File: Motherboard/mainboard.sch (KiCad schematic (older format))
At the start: 44 parts, among them IC1 BMX160, J1 Conn_01x01, J2 10118194-0001LF, J28 Conn_01x01, J29 Conn_01x01, J3 Micro_SD_Card, J30 Conn_01x01, J4 xf2m-2415-1a, J5 XF2M-1015-1A, SW1 KMR231NG LFS, U1 RFM95W-915S2, U2 ATSAMD51G_TQFN48, U4 TPS82740BSIPR, U6 MAX708RESA-T, U8 RFM95W-915S2, X1 ANTENNA_U.FL, X2 ANTENNA_U.FL

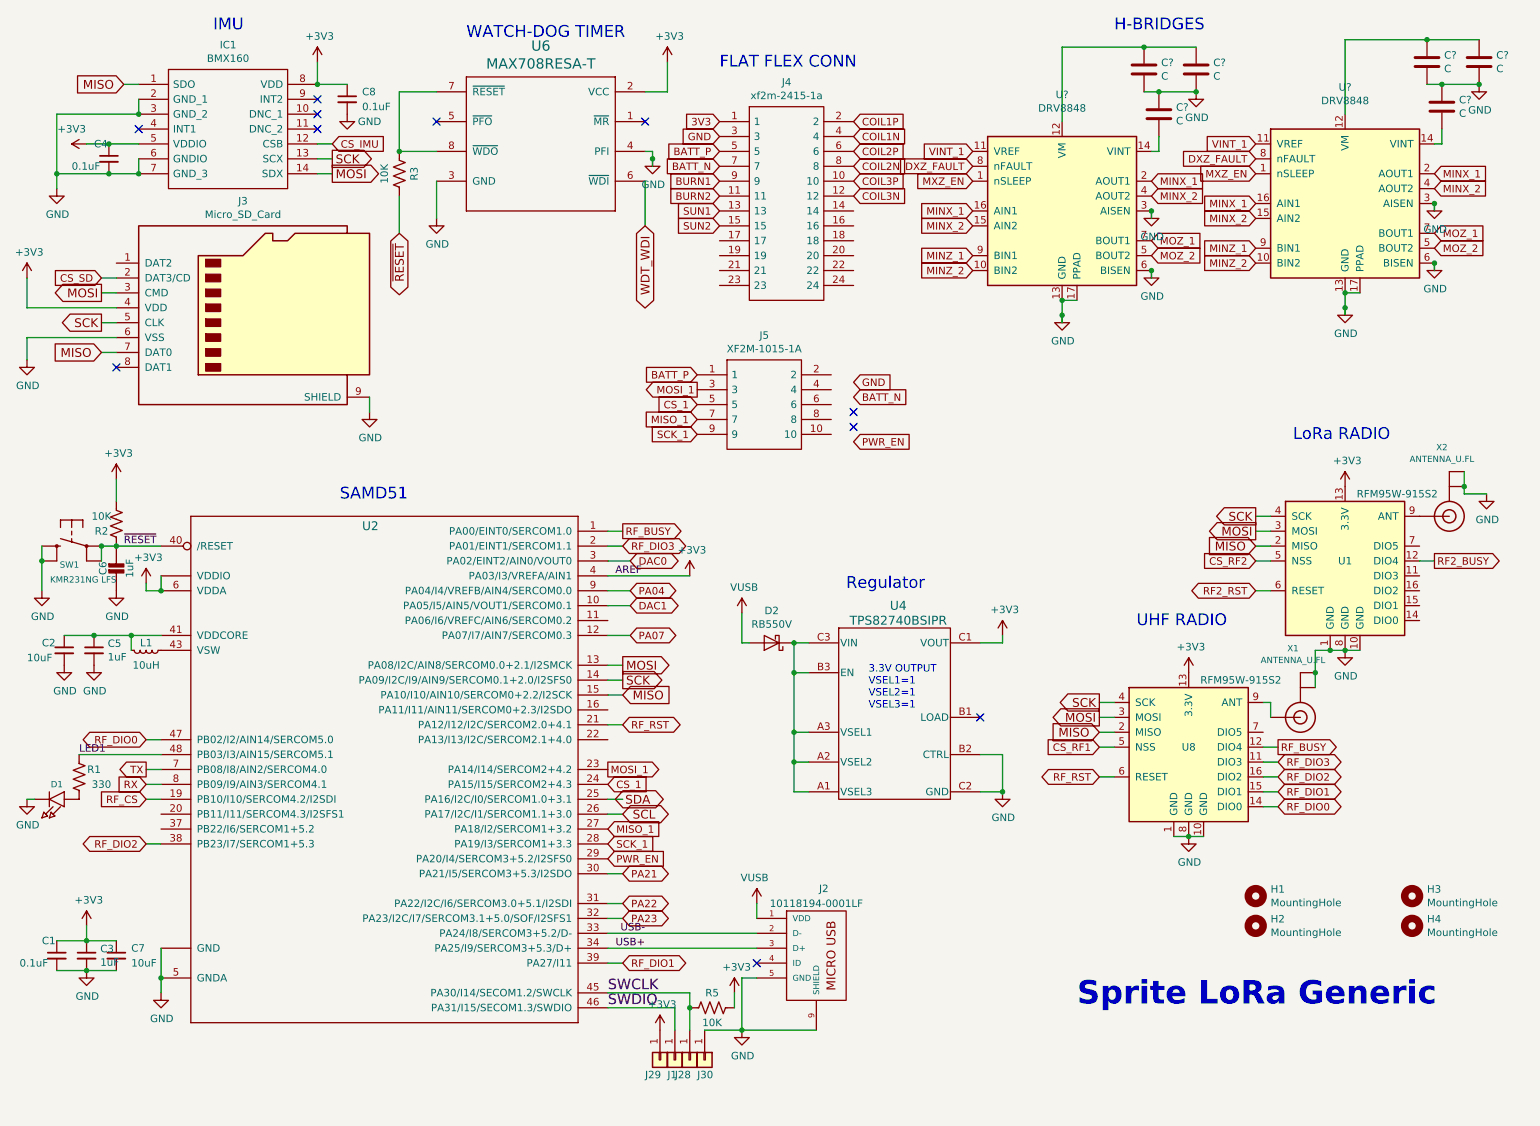
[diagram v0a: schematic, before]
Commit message: adding second I2C bus and fixing SPI pins
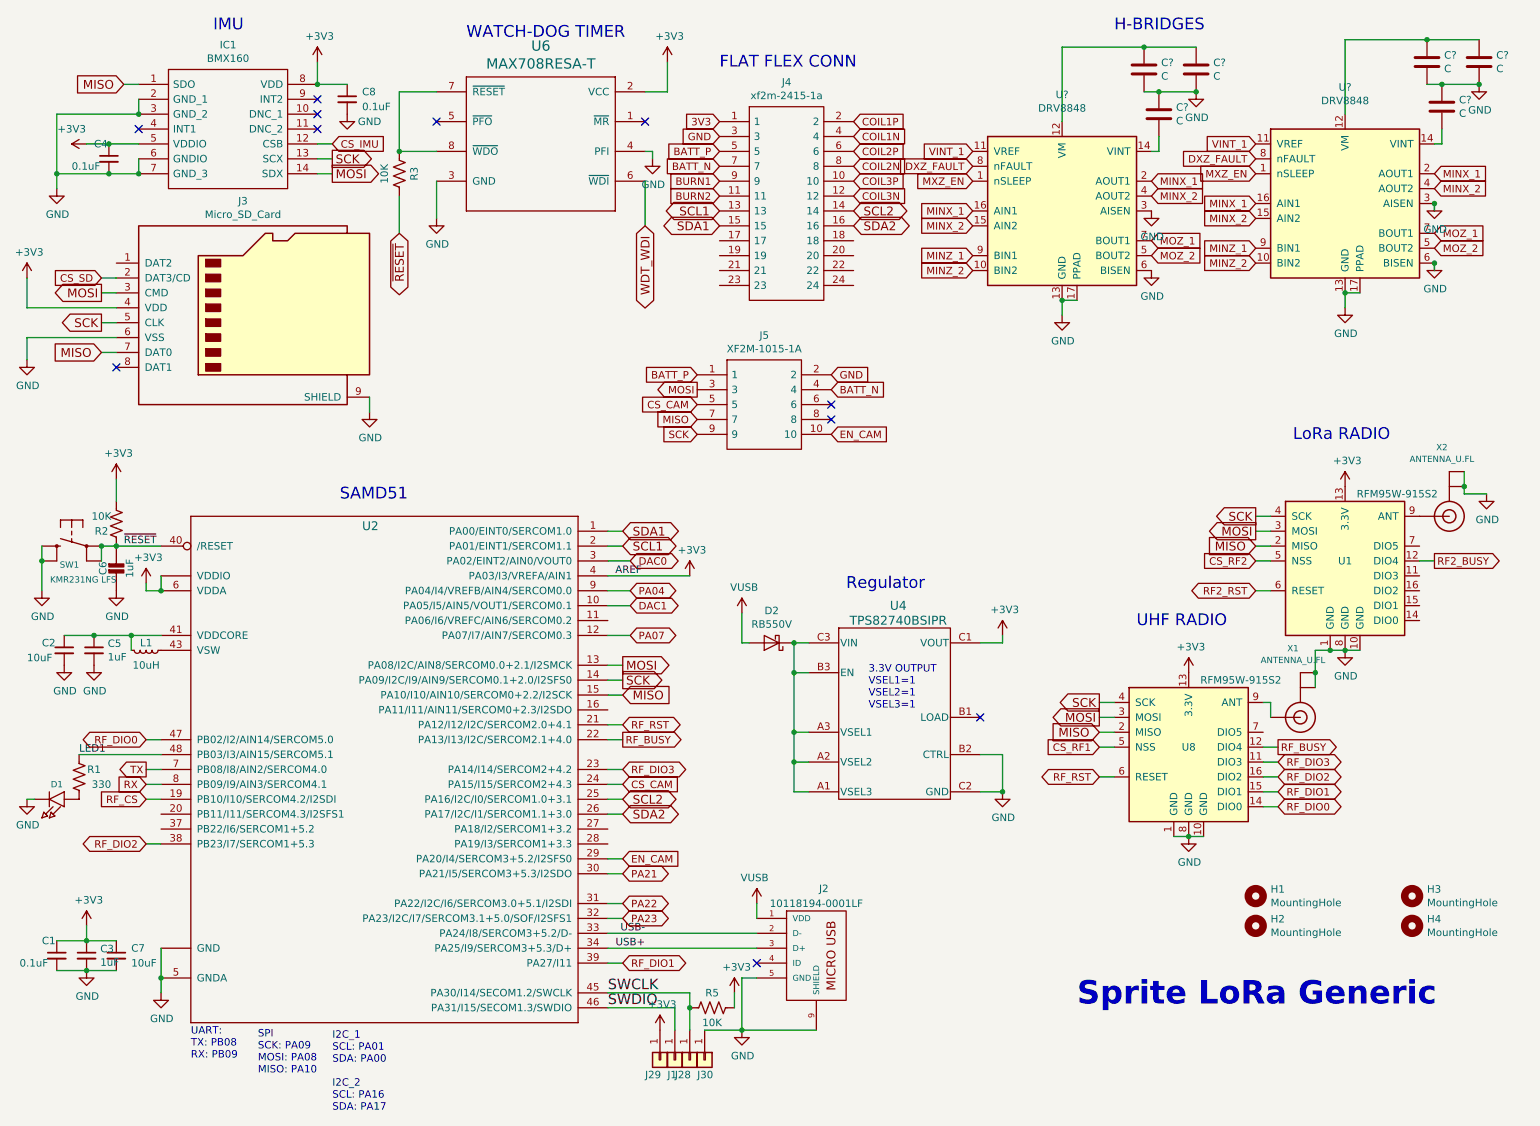
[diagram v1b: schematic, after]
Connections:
- net labels added: CS_CAM, EN_CAM, SCL1, SCL2, SDA1, SDA2
- net labels removed: CS_1, MISO_1, MOSI_1, PWR_EN, SCK_1, SCL, SDA, SUN1, SUN2
- wire segments 160 -> 159
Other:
- note added: "I2C_1\nSCL: PA01\nSDA: PA00\n\nI2C_2\nSCL: PA16\nSDA: PA17\n"
- note added: "SPI\nSCK: PA09\nMOSI: PA08\nMISO: PA10\n"
- note added: "UART:\nTX: PB08\nRX: PB09\n"
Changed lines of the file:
@@
 Text GLabel 1350 6100 0    50   BiDi ~ 0
 RF_DIO2
-Text GLabel 4550 4100 2    50   BiDi ~ 0
+Text GLabel 4550 5600 2    50   BiDi ~ 0
 RF_DIO3
-Text GLabel 4550 4000 2    50   Output ~ 0
+Text GLabel 4550 5400 2    50   Output ~ 0
 RF_BUSY
 Text GLabel 4550 6900 2    50   BiDi ~ 0
@@
 MOZ_2
 Wire Wire Line
-	7500 2600 7500 2550
-Wire Wire Line
 	7500 2550 7500 2450
-Connection ~ 7500 2550
 Wire Wire Line
 	7600 2450 7500 2450
@@
 	1    0    0    -1
 $EndComp
-Wire Wire Line
-	8100 1900 8100 1850
 $Comp
 L power:GND #PWR?
@@
 	1    0    0    -1
 $EndComp
-Wire Wire Line
-	8100 2300 8100 2250
 $Comp
 L Device:C C?
@@
 MOZ_2
 Wire Wire Line
-	9400 2550 9400 2500
-Wire Wire Line
 	9400 2500 9400 2400
-Connection ~ 9400 2500
 Wire Wire Line
 	9500 2400 9400 2400
@@
 Wire Wire Line
 	10000 2250 10000 2200
-Connection ~ 8100 1850
-Connection ~ 8100 2250
 Connection ~ 10000 1800
 Connection ~ 10000 2200
@@
 BATT_P
 Text GLabel 5050 3050 0    50   Output ~ 0
-MOSI_1
+MOSI
 Text GLabel 5050 3250 0    50   Input ~ 0
-MISO_1
+MISO
 Text GLabel 5050 3350 0    50   Input ~ 0
-SCK_1
-Text GLabel 6100 3400 2    50   Input ~ 0
-PWR_EN
-Text GLabel 6100 3000 2    50   Input ~ 0
+SCK
+Text GLabel 5950 3350 2    50   Input ~ 0
+EN_CAM
+Text GLabel 5950 2950 2    50   Input ~ 0
 GND
 Text GLabel 5050 3150 0    50   Input ~ 0
-CS_1
-Text GLabel 6100 3100 2    50   Input ~ 0
+CS_CAM
+Text GLabel 5950 3050 2    50   Input ~ 0
 BATT_N
-Text GLabel 4450 5600 2    50   Output ~ 0
-MOSI_1
-Text GLabel 4450 6100 2    50   Input ~ 0
-SCK_1
-Text GLabel 4450 6000 2    50   Input ~ 0
-MISO_1
-Text GLabel 4450 5700 2    50   Input ~ 0
-CS_1
-NoConn ~ 6100 3200
-NoConn ~ 6100 3300
+Text GLabel 4550 5700 2    50   Input ~ 0
+CS_CAM
+NoConn ~ 5950 3150
+NoConn ~ 5950 3250
 Connection ~ 1450 7000
 Wire Wire Line
@@
 	4450 6300 4550 6300
 Wire Wire Line
-	4450 5900 4550 5900
+	4450 5800 4550 5800
 Wire Wire Line
 	4450 5300 4550 5300
@@
 	4450 4200 4600 4200
 Wire Wire Line
-	4550 4100 4450 4100
-Wire Wire Line
-	4550 4000 4450 4000
-Wire Wire Line
-	4550 5800 4450 5800
+	4550 5600 4450 5600
+Wire Wire Line
+	4550 5400 4450 5400
+Wire Wire Line
+	4550 5900 4450 5900
 $Comp
 L mainboard-rescue:ATSAMD51G_TQFN48- U2
@@
 	1    0    0    -1
 $EndComp
-Text GLabel 4500 5800 2    59   BiDi ~ 0
-SDA
-Text GLabel 4450 6200 2    50   Input ~ 0
-PWR_EN
-Text GLabel 4550 5900 2    59   BiDi ~ 0
-SCL
+Text GLabel 4550 6200 2    50   Input ~ 0
+EN_CAM
+Text GLabel 4550 5800 2    59   BiDi ~ 0
+SCL2
 Text GLabel 5200 1250 0    50   Input ~ 0
 3V3
@@
 Text GLabel 5200 1750 0    50   Input ~ 0
 BURN2
-Text GLabel 5200 1850 0    50   Input ~ 0
-SUN1
-Text GLabel 5200 1950 0    50   Input ~ 0
-SUN2
 Text GLabel 6100 1250 2    50   Input ~ 0
 COIL1P
@@
 Wire Wire Line
 	4750 1450 4750 1500
-Connection ~ 4750 1500
-Wire Wire Line
-	4750 1500 4750 1550
 Text GLabel 6100 1450 2    50   Input ~ 0
 COIL2P
@@
 Text GLabel 6100 1750 2    50   Input ~ 0
 COIL3N
+Text GLabel 4550 5900 2    59   BiDi ~ 0
+SDA2
+Wire Wire Line
+	4450 4000 4550 4000
+Wire Wire Line
+	4550 4100 4450 4100
+Text GLabel 4550 4000 2    59   BiDi ~ 0
+SDA1
+Text GLabel 4550 4100 2    59   BiDi ~ 0
+SCL1
+Wire Wire Line
+	4550 5700 4450 5700
+Text Notes 1650 7550 0    50   ~ 0
+UART:\nTX: PB08\nRX: PB09\n
+Text Notes 2100 7650 0    50   ~ 0
+SPI\nSCK: PA09\nMOSI: PA08\nMISO: PA10\n
+Text Notes 2600 7900 0    50   ~ 0
+I2C_1\nSCL: PA01\nSDA: PA00\n\nI2C_2\nSCL: PA16\nSDA: PA17\n
+Text GLabel 5200 1950 0    59   BiDi ~ 0
+SDA1
+Text GLabel 5200 1850 0    59   BiDi ~ 0
+SCL1
+Text GLabel 6100 1850 2    59   BiDi ~ 0
+SCL2
+Text GLabel 6100 1950 2    59   BiDi ~ 0
+SDA2
+Wire Wire Line
+	4550 6200 4450 6200
 $EndSCHEMATC

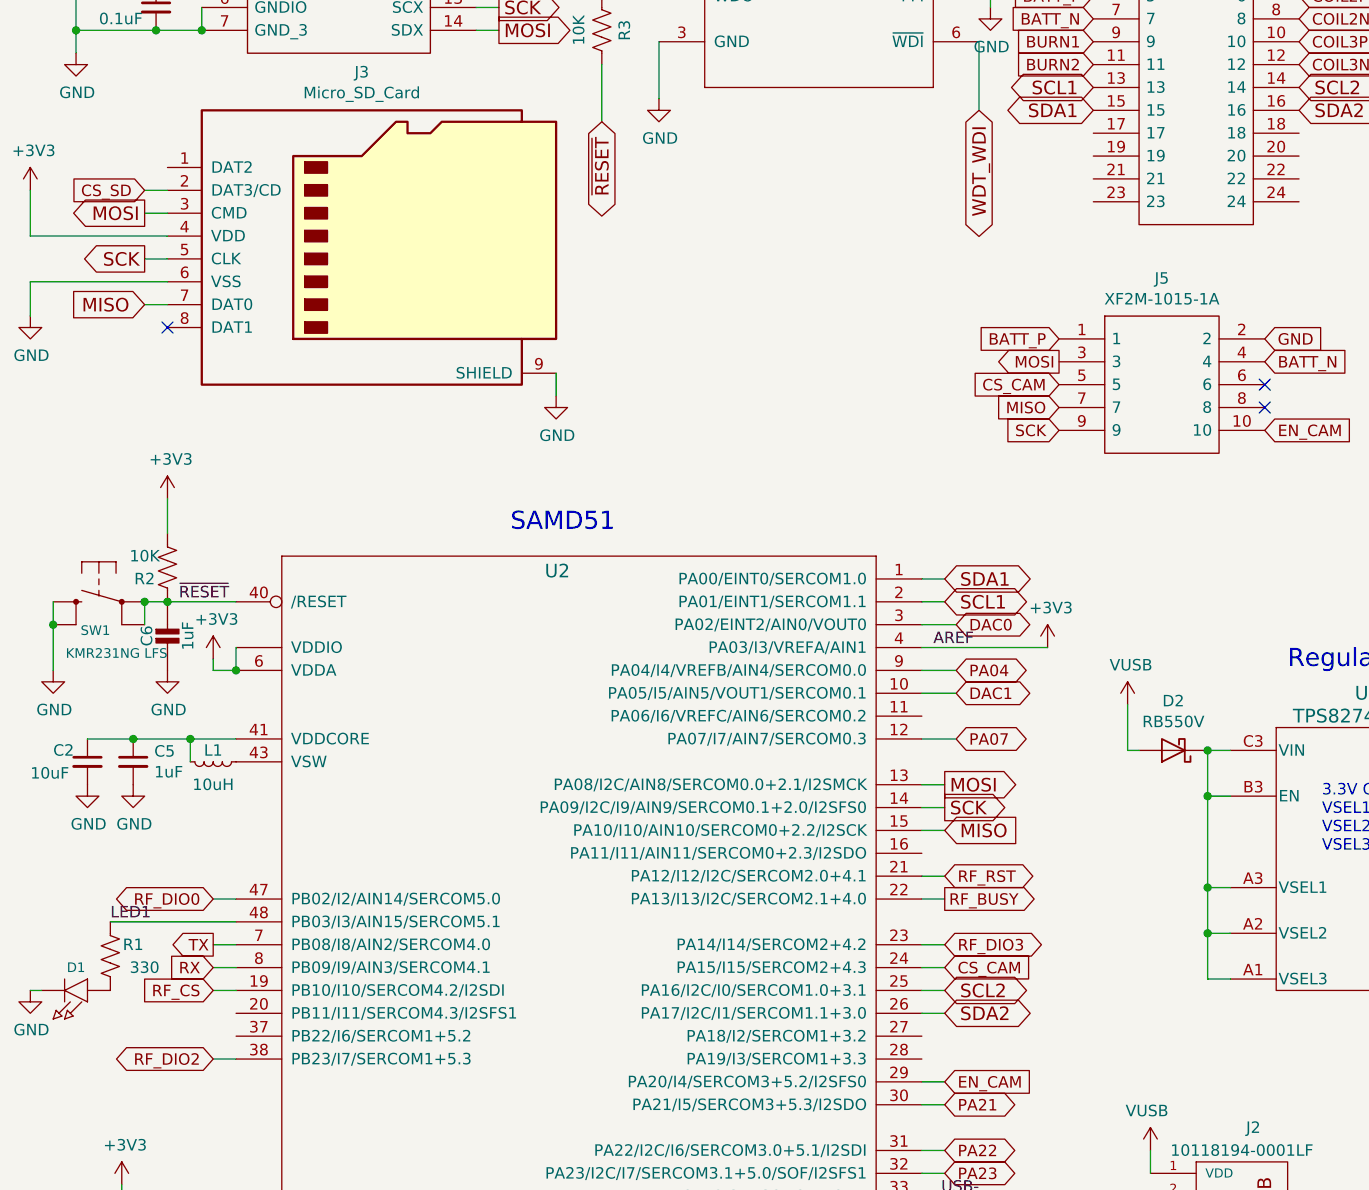
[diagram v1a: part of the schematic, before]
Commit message: adding pull-up resistors to I2C
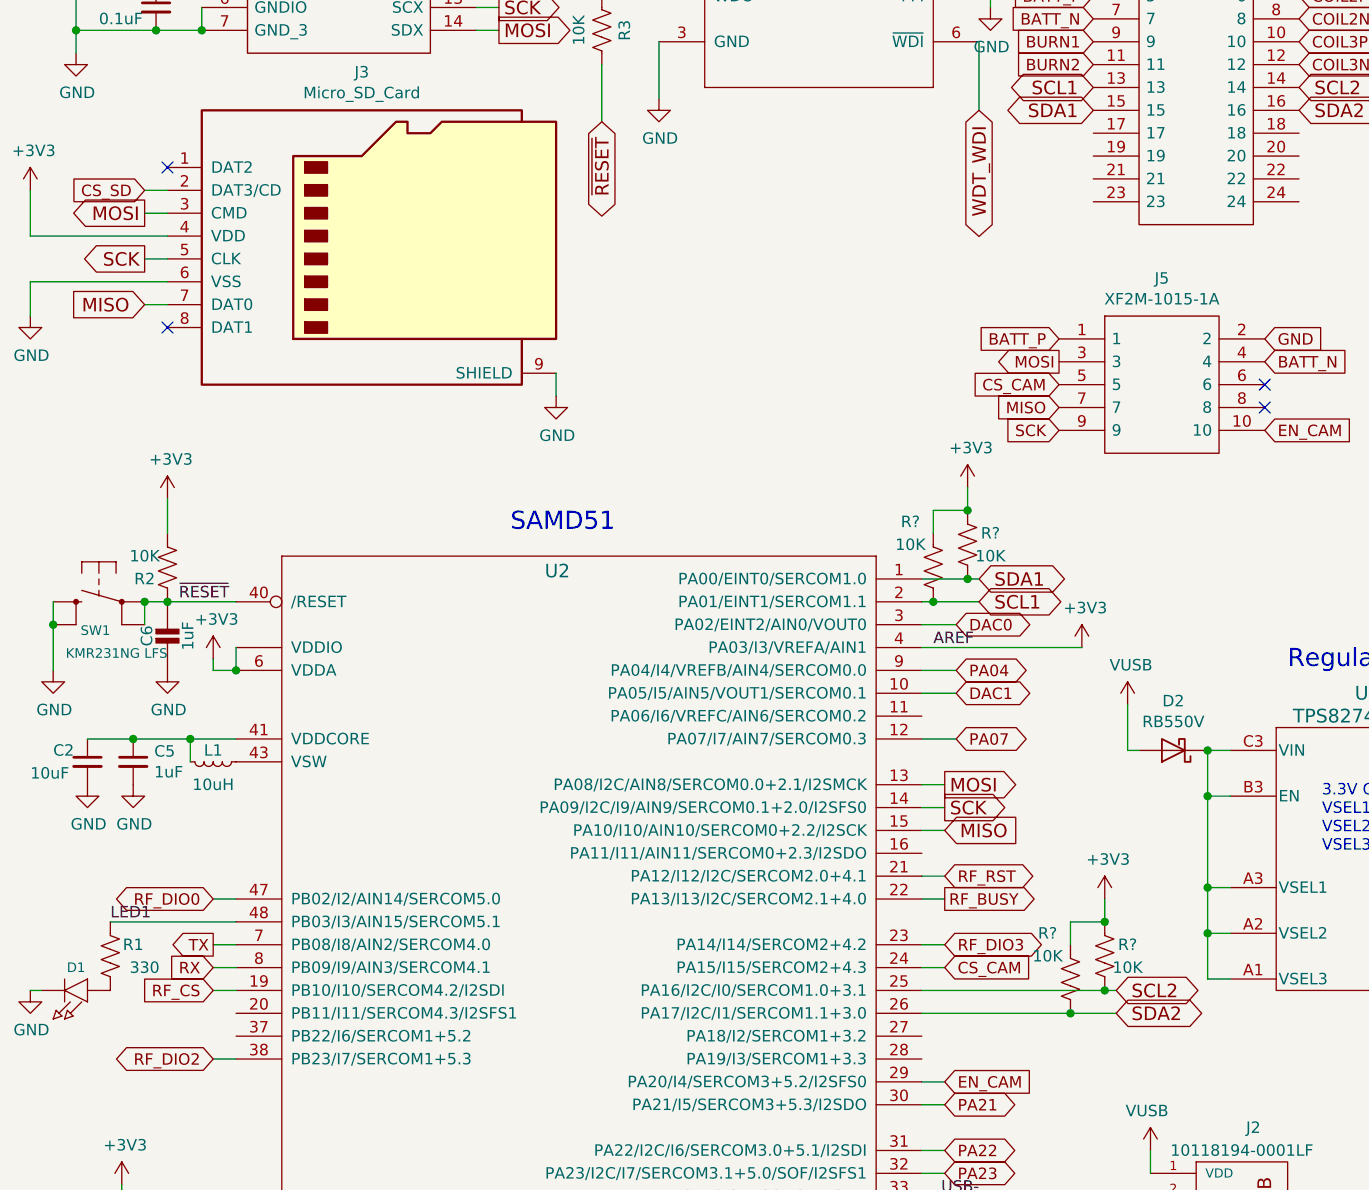
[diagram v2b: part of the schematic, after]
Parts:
- added R? (x4): 10K, Resistor_SMD:R_0402_1005Metric, symbol Device:R_US
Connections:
- net +3V3: now also R?.2, R?.2, R?.2, R?.2
- net SCL1: now also R?.1
- net SCL2: now also R?.1
- net SDA1: now also R?.1
- net SDA2: now also R?.1
- no-connect marks 11 -> 12
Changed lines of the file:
@@
 L power:+3V3 #PWR0108
 U 1 1 5D7F36A0
-P 5000 4300
-F 0 "#PWR0108" H 5000 4150 50  0001 C CNN
-F 1 "+3V3" H 5015 4473 50  0000 C CNN
-F 2 "" H 5000 4300 50  0001 C CNN
-F 3 "" H 5000 4300 50  0001 C CNN
-	1    5000 4300
+P 5150 4300
+F 0 "#PWR0108" H 5150 4150 50  0001 C CNN
+F 1 "+3V3" H 5165 4473 50  0000 C CNN
+F 2 "" H 5150 4300 50  0001 C CNN
+F 3 "" H 5150 4300 50  0001 C CNN
+	1    5150 4300
 	1    0    0    -1
 $EndComp
@@
 	4450 6300 4550 6300
 Wire Wire Line
-	4450 5800 4550 5800
+	4450 5800 5250 5800
 Wire Wire Line
 	4450 5300 4550 5300
@@
 	4450 4400 4600 4400
 Wire Wire Line
-	4450 4300 5000 4300
+	4450 4300 5150 4300
 Wire Wire Line
 	4450 4200 4600 4200
@@
 	4550 5400 4450 5400
 Wire Wire Line
-	4550 5900 4450 5900
+	5300 5900 5100 5900
 $Comp
 L mainboard-rescue:ATSAMD51G_TQFN48- U2
@@
 Text GLabel 4550 6200 2    50   Input ~ 0
 EN_CAM
-Text GLabel 4550 5800 2    59   BiDi ~ 0
+Text GLabel 5300 5800 2    59   BiDi ~ 0
 SCL2
 Text GLabel 5200 1250 0    50   Input ~ 0
@@
 Text GLabel 6100 1750 2    50   Input ~ 0
 COIL3N
-Text GLabel 4550 5900 2    59   BiDi ~ 0
+Text GLabel 5300 5900 2    59   BiDi ~ 0
 SDA2
 Wire Wire Line
-	4450 4000 4550 4000
-Wire Wire Line
-	4550 4100 4450 4100
-Text GLabel 4550 4000 2    59   BiDi ~ 0
+	4450 4000 4650 4000
+Wire Wire Line
+	4700 4100 4500 4100
+Text GLabel 4700 4000 2    59   BiDi ~ 0
 SDA1
-Text GLabel 4550 4100 2    59   BiDi ~ 0
+Text GLabel 4700 4100 2    59   BiDi ~ 0
 SCL1
 Wire Wire Line
@@
 Wire Wire Line
 	4550 6200 4450 6200
+$Comp
+L Device:R_US R?
+U 1 1 5DB0C8A9
+P 4500 3950
+F 0 "R?" H 4600 3750 50  0000 C CNN
+F 1 "10K" H 4600 3850 50  0000 C CNN
+F 2 "Resistor_SMD:R_0402_1005Metric" V 4540 3940 50  0001 C CNN
+F 3 "~" H 4500 3950 50  0001 C CNN
+	1    4500 3950
+	-1   0    0    1
+$EndComp
+Connection ~ 4500 4100
+Wire Wire Line
+	4500 4100 4450 4100
+$Comp
+L Device:R_US R?
+U 1 1 5DB0D4A3
+P 4650 3850
+F 0 "R?" H 4550 3800 50  0000 C CNN
+F 1 "10K" H 4550 3900 50  0000 C CNN
+F 2 "Resistor_SMD:R_0402_1005Metric" V 4690 3840 50  0001 C CNN
+F 3 "~" H 4650 3850 50  0001 C CNN
+	1    4650 3850
+	-1   0    0    1
+$EndComp
+Connection ~ 4650 4000
+Wire Wire Line
+	4650 4000 4700 4000
+$Comp
+L power:+3V3 #PWR?
+U 1 1 5DB0E5CD
+P 4650 3600
+F 0 "#PWR?" H 4650 3450 50  0001 C CNN
+F 1 "+3V3" H 4665 3773 50  0000 C CNN
+F 2 "" H 4650 3600 50  0001 C CNN
+F 3 "" H 4650 3600 50  0001 C CNN
+	1    4650 3600
+	1    0    0    -1
+$EndComp
+Wire Wire Line
+	4650 3600 4650 3700
+Wire Wire Line
+	4500 3800 4500 3700
+Wire Wire Line
+	4500 3700 4650 3700
+Connection ~ 4650 3700
+NoConn ~ 1150 2200
+$Comp
+L Device:R_US R?
+U 1 1 5DB33981
+P 5100 5750
+F 0 "R?" H 5200 5550 50  0000 C CNN
+F 1 "10K" H 5200 5650 50  0000 C CNN
+F 2 "Resistor_SMD:R_0402_1005Metric" V 5140 5740 50  0001 C CNN
+F 3 "~" H 5100 5750 50  0001 C CNN
+	1    5100 5750
+	-1   0    0    1
+$EndComp
+$Comp
+L Device:R_US R?
+U 1 1 5DB33987
+P 5250 5650
+F 0 "R?" H 5150 5600 50  0000 C CNN
+F 1 "10K" H 5150 5700 50  0000 C CNN
+F 2 "Resistor_SMD:R_0402_1005Metric" V 5290 5640 50  0001 C CNN
+F 3 "~" H 5250 5650 50  0001 C CNN
+	1    5250 5650
+	-1   0    0    1
+$EndComp
+$Comp
+L power:+3V3 #PWR?
+U 1 1 5DB3398D
+P 5250 5400
+F 0 "#PWR?" H 5250 5250 50  0001 C CNN
+F 1 "+3V3" H 5265 5573 50  0000 C CNN
+F 2 "" H 5250 5400 50  0001 C CNN
+F 3 "" H 5250 5400 50  0001 C CNN
+	1    5250 5400
+	1    0    0    -1
+$EndComp
+Wire Wire Line
+	5250 5400 5250 5500
+Wire Wire Line
+	5100 5600 5100 5500
+Wire Wire Line
+	5100 5500 5250 5500
+Connection ~ 5250 5500
+Connection ~ 5100 5900
+Wire Wire Line
+	5100 5900 4450 5900
+Connection ~ 5250 5800
+Wire Wire Line
+	5250 5800 5300 5800
 $EndSCHEMATC
